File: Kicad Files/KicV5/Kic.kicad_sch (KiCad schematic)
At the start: 19 parts, among them J1 Power, J2 Digital/PWM, J3 Analog, J4 Digital/PWM, U5 MCP41100

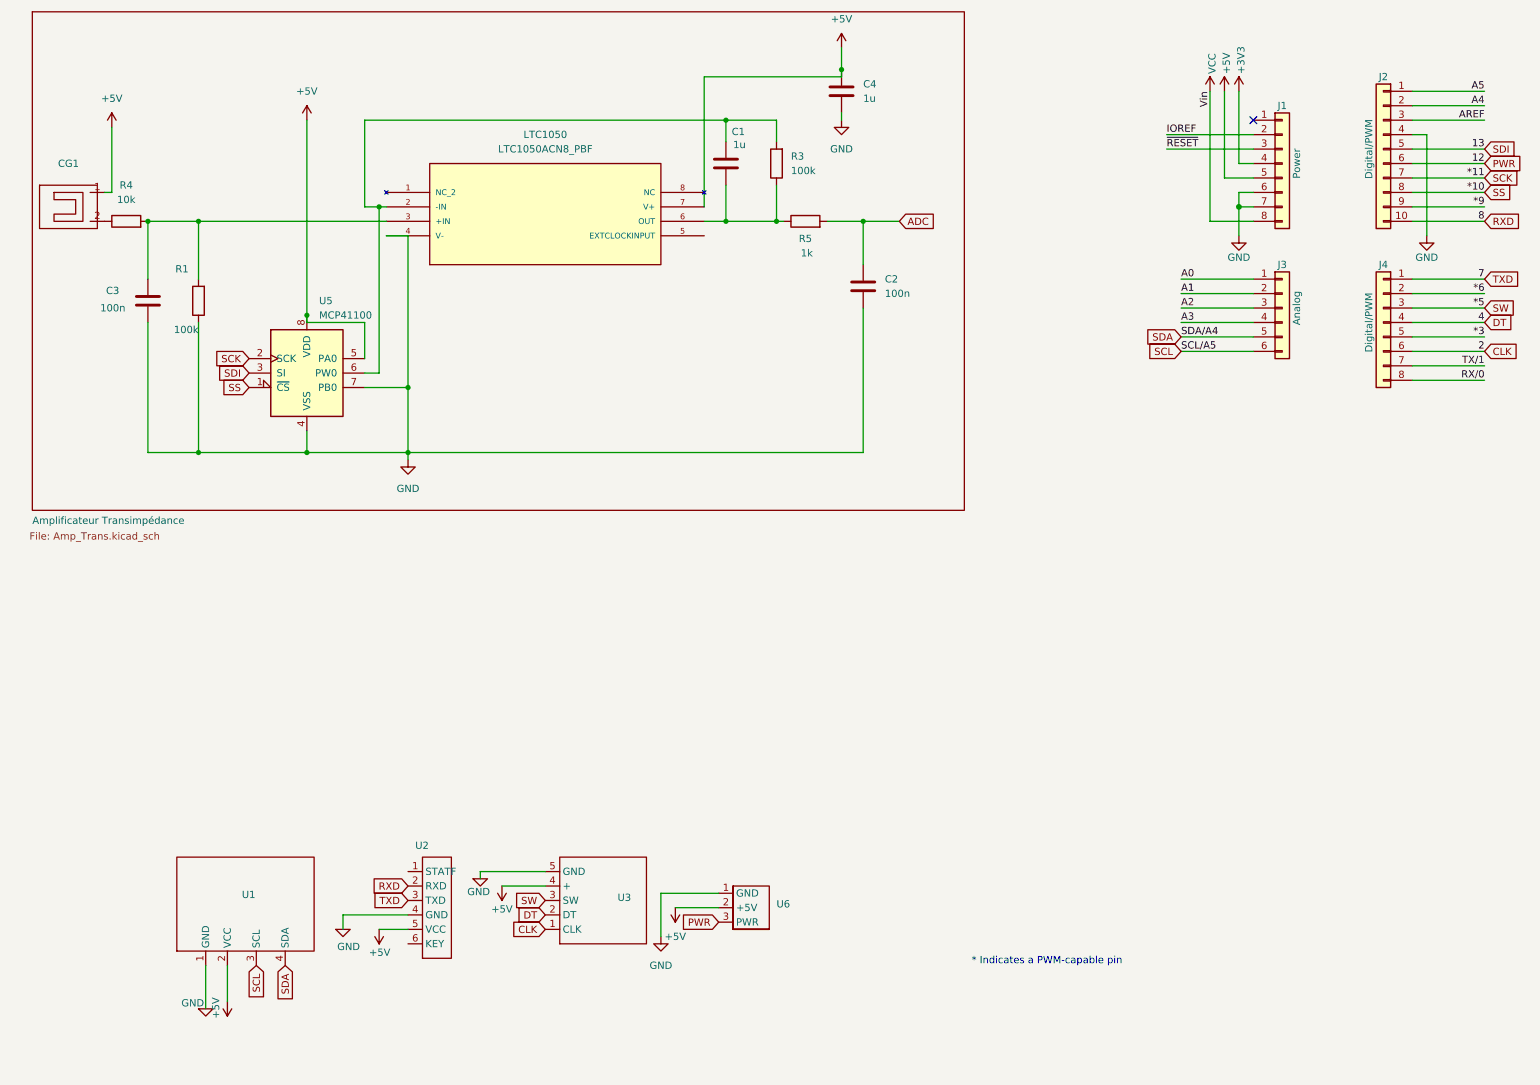
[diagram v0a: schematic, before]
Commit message: Ajout d'une V5 des fichiers Kicadet mise à jour du fichier Arduino avvec l'ajout de code pour les différents modules
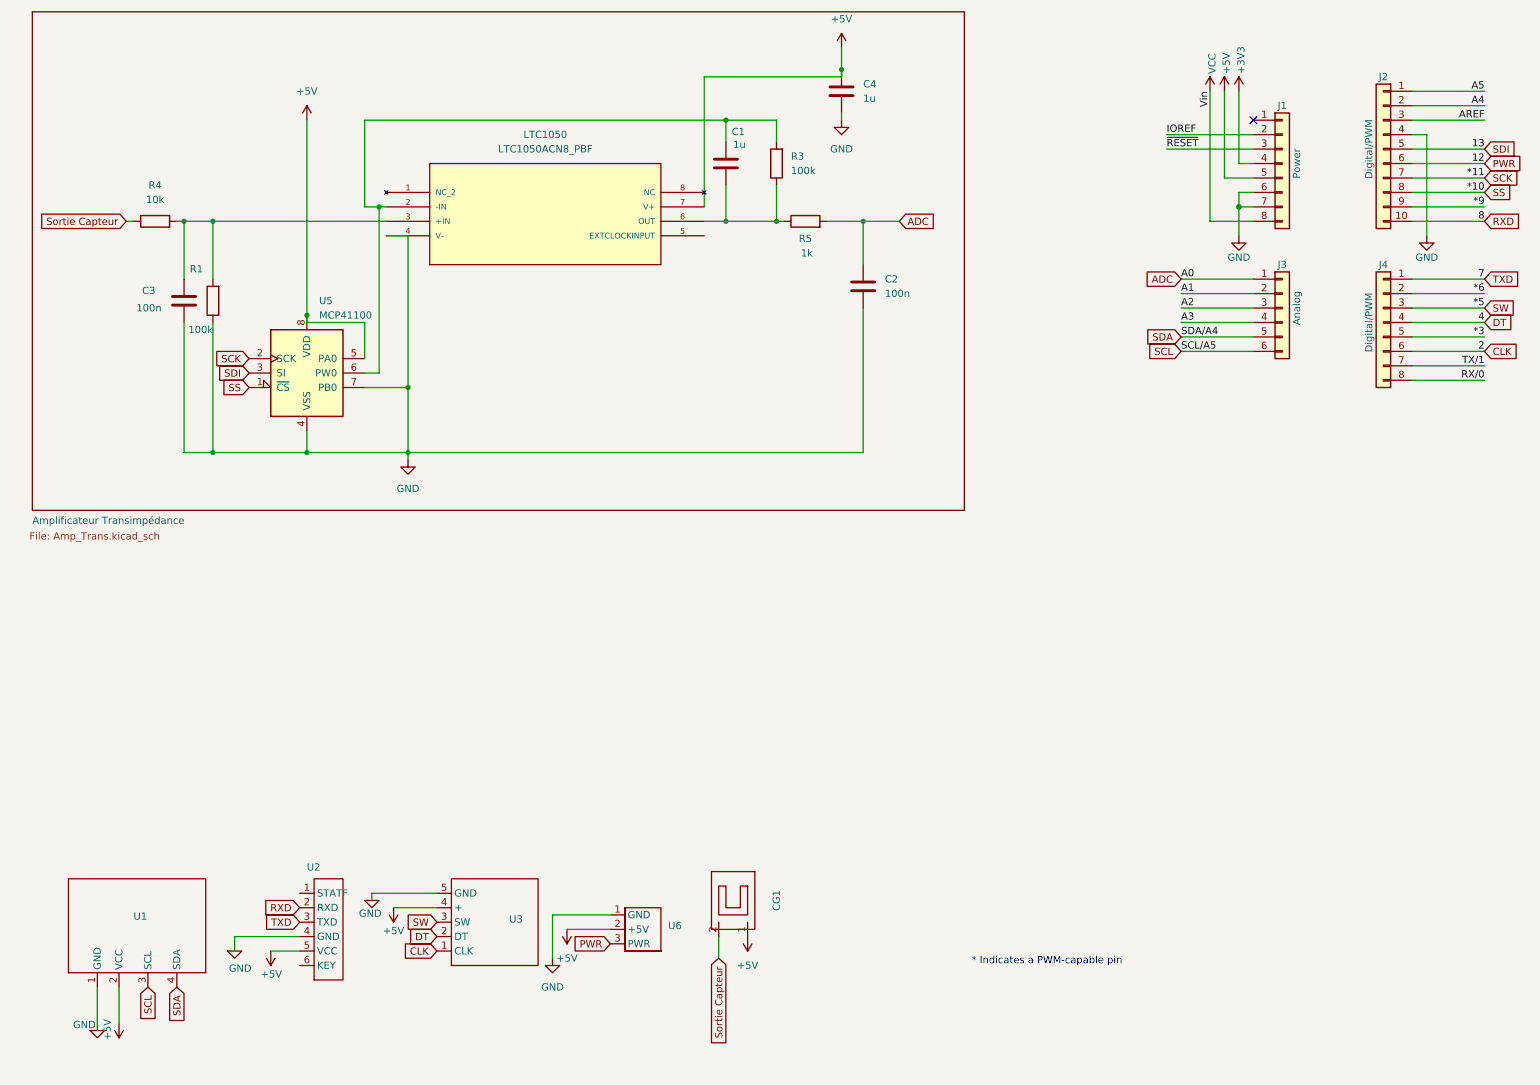
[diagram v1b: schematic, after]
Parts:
- U5: footprint LTC1050ACN8_PBF:PDIP-8_N -> My_footprints_Librairy:MCP4110
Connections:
- net A0 is gone; now on net ADC: J3.1 (Pin_1)
- net Sortie Capteur: now reaches CG1.2, R4.1
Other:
- moved on the sheet: C3, CG1, R1, R4, U1, U2, U3, U6
